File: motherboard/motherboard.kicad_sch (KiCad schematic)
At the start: 17 parts, among them J1 Conn_01x12_MountingPin, J2 Conn_01x12_MountingPin, J3 Conn_01x12_MountingPin, J4 Conn_01x12_MountingPin, J5 Conn_01x12_MountingPin, J6 Conn_01x12_MountingPin, J7 USB_C_Receptacle_USB2.0, U1 SRV05-4

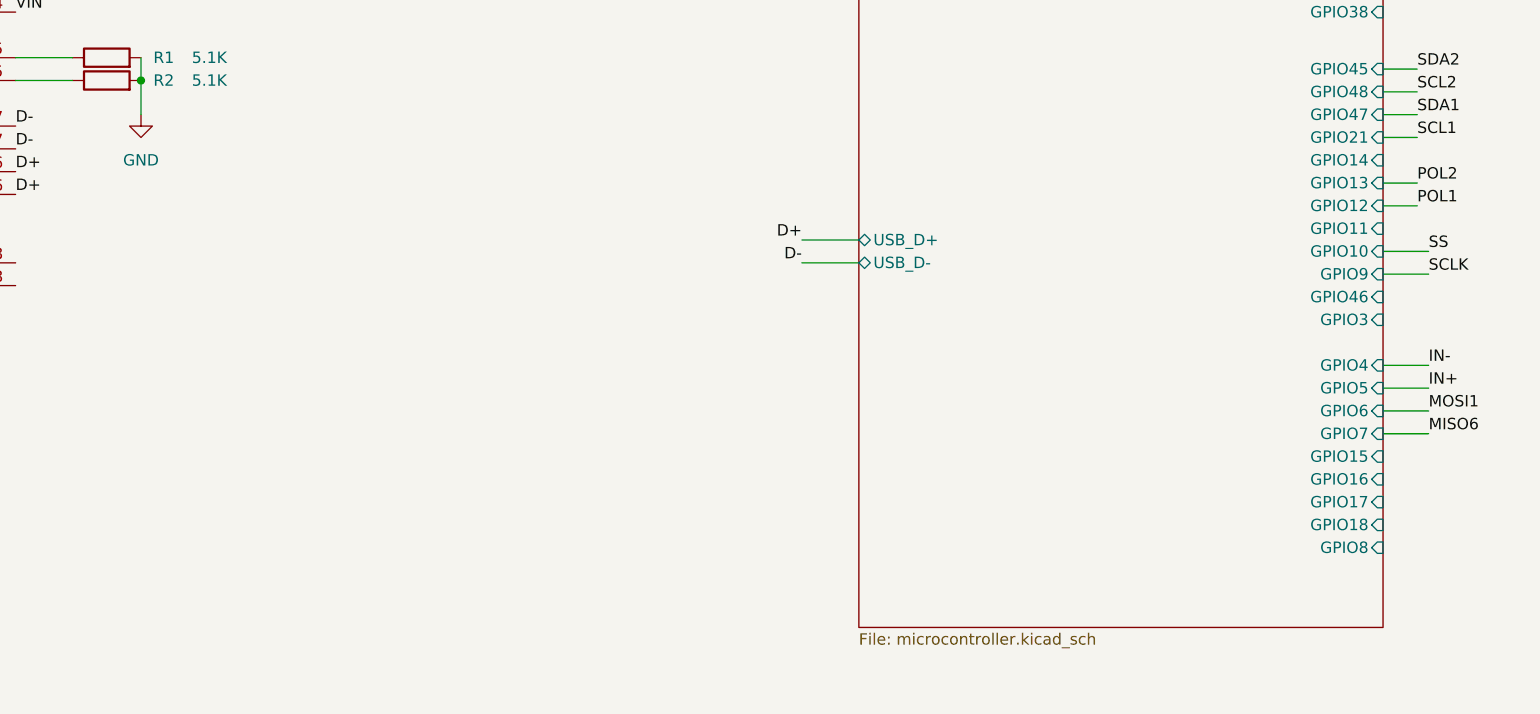
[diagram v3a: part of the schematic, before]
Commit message: motherboard low pass filter
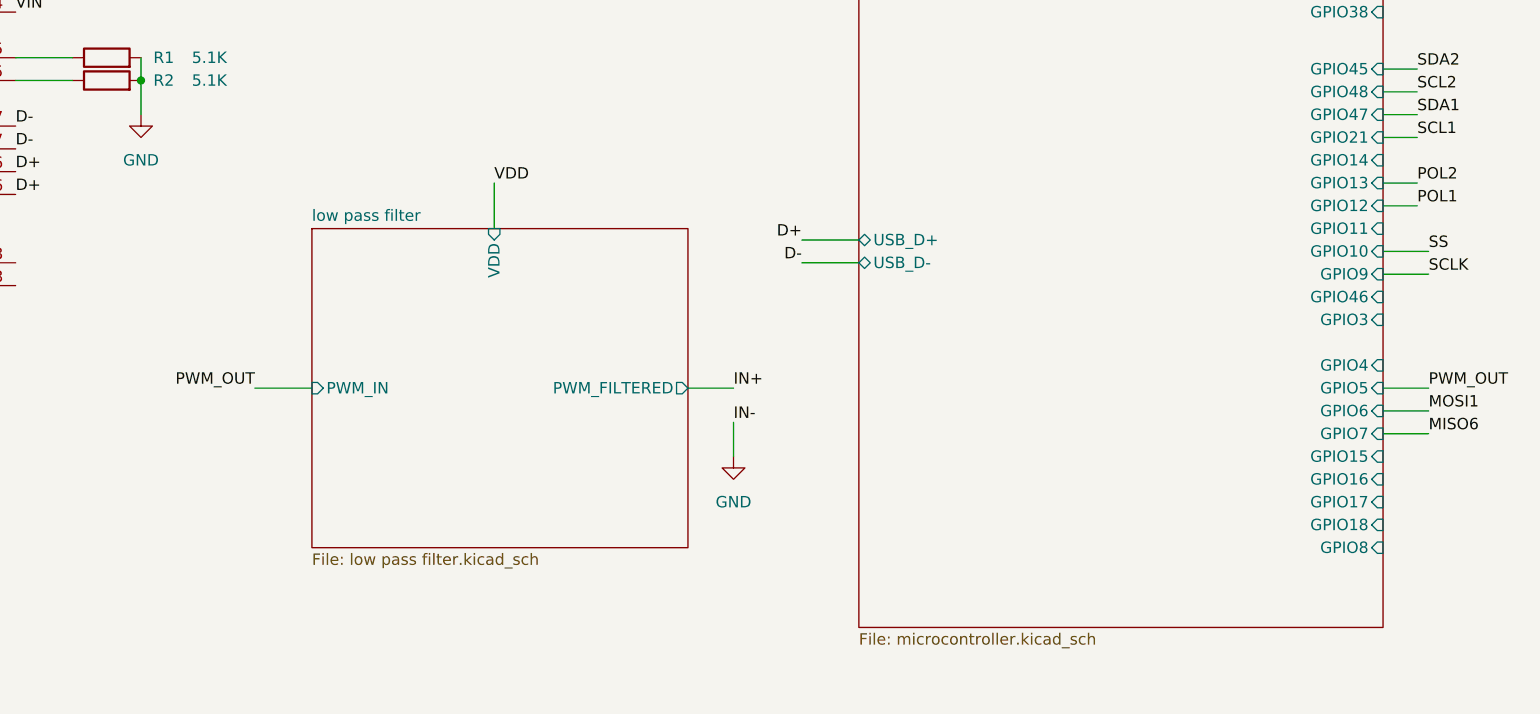
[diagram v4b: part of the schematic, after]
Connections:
- net IN- is gone; now on net GND: J1.5 (Pin_5), J2.5 (Pin_5), J3.5 (Pin_5), J4.5 (Pin_5), J5.5 (Pin_5), J6.5 (Pin_5)
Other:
- added sheet low pass filter (low pass filter.kicad_sch)
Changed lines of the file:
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@@
+    (stroke (width 0) (type default))
+  )
+  (wire (pts (xy 157.48 102.87) (xy 157.48 107.95))
     (stroke (width 0) (type default))
   )
@@
     (stroke (width 0) (type default))
   )
+  (wire (pts (xy 184.15 129.54) (xy 184.15 133.35))
+    (stroke (width 0) (type default))
+  )
   (wire (pts (xy 50.8 156.21) (xy 46.99 156.21))
     (stroke (width 0) (type default))
@@
     (stroke (width 0) (type default))
   )
+  (wire (pts (xy 179.07 125.73) (xy 184.15 125.73))
+    (stroke (width 0) (type default))
+  )
   (wire (pts (xy 236.22 34.29) (xy 241.3 34.29))
     (stroke (width 0) (type default))
@@
     (stroke (width 0) (type default))
   )
-  (wire (pts (xy 256.54 123.19) (xy 261.62 123.19))
+  (wire (pts (xy 130.81 125.73) (xy 137.16 125.73))
     (stroke (width 0) (type default))
   )
@@
     (effects (font (size 1.27 1.27)) (justify right bottom))
   )
+  (label "IN+" (at 184.15 125.73 0) (fields_autoplaced)
+    (effects (font (size 1.27 1.27)) (justify left bottom))
+  )
   (label "SCL1" (at 260.35 97.79 0) (fields_autoplaced)
     (effects (font (size 1.27 1.27)) (justify left bottom))
@@
     (effects (font (size 1.27 1.27)) (justify right bottom))
   )
-  (label "IN-" (at 261.62 123.19 0) (fields_autoplaced)
+  (label "IN-" (at 184.15 129.54 0) (fields_autoplaced)
     (effects (font (size 1.27 1.27)) (justify left bottom))
   )
@@
     (effects (font (size 1.27 1.27)) (justify right bottom))
   )
-  (label "IN+" (at 261.62 125.73 0) (fields_autoplaced)
+  (label "PWM_OUT" (at 261.62 125.73 0) (fields_autoplaced)
     (effects (font (size 1.27 1.27)) (justify left bottom))
   )
@@
     (effects (font (size 1.27 1.27)) (justify right bottom))
   )
+  (label "PWM_OUT" (at 130.81 125.73 180) (fields_autoplaced)
+    (effects (font (size 1.27 1.27)) (justify right bottom))
+  )
   (label "VIN" (at 104.14 83.82 0) (fields_autoplaced)
     (effects (font (size 1.27 1.27)) (justify left bottom))
@@
   )
   (label "POL1" (at 260.35 105.41 0) (fields_autoplaced)
+    (effects (font (size 1.27 1.27)) (justify left bottom))
+  )
+  (label "VDD" (at 157.48 102.87 0) (fields_autoplaced)
     (effects (font (size 1.27 1.27)) (justify left bottom))
   )
@@
         (path "/e63e39d7-6ac0-4ffd-8aa3-1841a4541b55"
           (reference "U1") (unit 1)
+        )
+      )
+    )
+  )
+  (symbol (lib_name "GND_2") (lib_id "power:GND") (at 184.15 133.35 0) (unit 1)
+    (in_bom yes) (on_board yes) (dnp no) (fields_autoplaced)
+    (property "Reference" "#PWR032" (at 184.15 139.7 0)
+      (effects (font (size 1.27 1.27)) hide)
+    )
+    (property "Value" "GND" (at 184.15 138.43 0)
+      (effects (font (size 1.27 1.27)))
+    )
+    (property "Footprint" "" (at 184.15 133.35 0)
+      (effects (font (size 1.27 1.27)) hide)
+    )
+    (property "Datasheet" "" (at 184.15 133.35 0)
+      (effects (font (size 1.27 1.27)) hide)
+    )
+    (pin "1")
+    (instances
+      (project "motherboard"
+        (path "/e63e39d7-6ac0-4ffd-8aa3-1841a4541b55"
+          (reference "#PWR032") (unit 1)
         )
       )
@@
       (effects (font (size 1.27 1.27)) (justify right))
     )
+    (instances
+      (project "motherboard"
+        (path "/e63e39d7-6ac0-4ffd-8aa3-1841a4541b55" (page "4"))
+      )
+    )
+  )
+  (sheet (at 137.16 107.95) (size 41.91 35.56) (fields_autoplaced)
+    (stroke (width 0.1524) (type solid))
+    (fill (color 0 0 0 0.0000))
+    (property "Sheetname" "low pass filter" (at 137.16 107.2384 0)
+      (effects (font (size 1.27 1.27)) (justify left bottom))
+    )
+    (property "Sheetfile" "low pass filter.kicad_sch" (at 137.16 144.0946 0)
+      (effects (font (size 1.27 1.27)) (justify left top))
+    )
+    (pin "PWM_IN" input (at 137.16 125.73 180)
+      (effects (font (size 1.27 1.27)) (justify left))
+    )
+    (pin "PWM_FILTERED" output (at 179.07 125.73 0)
+      (effects (font (size 1.27 1.27)) (justify right))
+    )
+    (pin "VDD" input (at 157.48 107.95 90)
+      (effects (font (size 1.27 1.27)) (justify right))
+    )
